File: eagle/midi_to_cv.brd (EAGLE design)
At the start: 100 x 80 mm, 73 parts, among them IC1 TL084P, IC2 4067N, IC3 4067N, IC4 TL072P, U1 ATMEGA328P_PDIP, U4 4584N

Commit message: parts basically on board and 072 powered
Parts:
- removed IC2, IC3: 4067N, 40xx:DIL24-6
- moved R27 249.5 mm to (91.4, 16.5)
- moved R29 249.5 mm to (72.4, 14.0)
- moved R28 242.3 mm to (72.4, 11.4)
- moved R18 238.0 mm to (91.4, 14.0)
- moved R10 233.4 mm to (91.4, 19.1), turned to 180 degrees
- moved R26 222.5 mm to (55.9, 6.35)
- moved R17 221.0 mm to (72.4, 8.89)
- moved R9 218.5 mm to (62.2, 20.3), turned to 180 degrees
- moved LED2 212.4 mm to (81.3, 20.3), turned to 180 degrees
- moved IC4 208.5 mm to (87.6, 7.62)
- moved R19 197.5 mm to (40.6, 38.1)
- moved LED1 189.2 mm to (72.4, 3.81), turned to 180 degrees
- moved MOUT_P5 188.9 mm to (43.2, 34.3)
- moved R23 174.7 mm to (3.81, 14.0), turned to 90 degrees
- moved MOUT_P4 170.2 mm to (3.81, 22.9)
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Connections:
- removed net V+: IC4.8
- removed net V-: IC4.4
- net +5V: now also IC4.8; no longer IC2.24, IC3.24
- net GND: now also IC4.4; no longer IC2.12, IC3.12

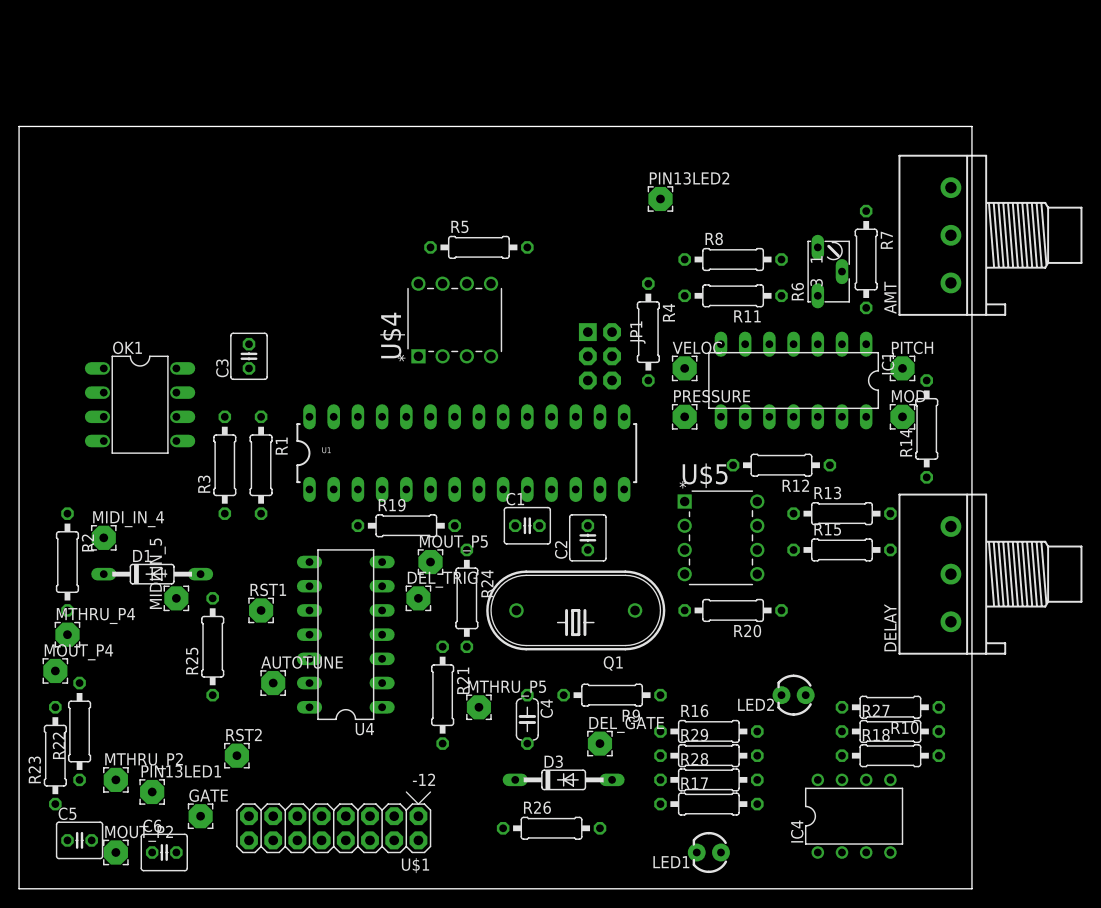
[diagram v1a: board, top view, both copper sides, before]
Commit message: swapped some gates and rearranged to layout
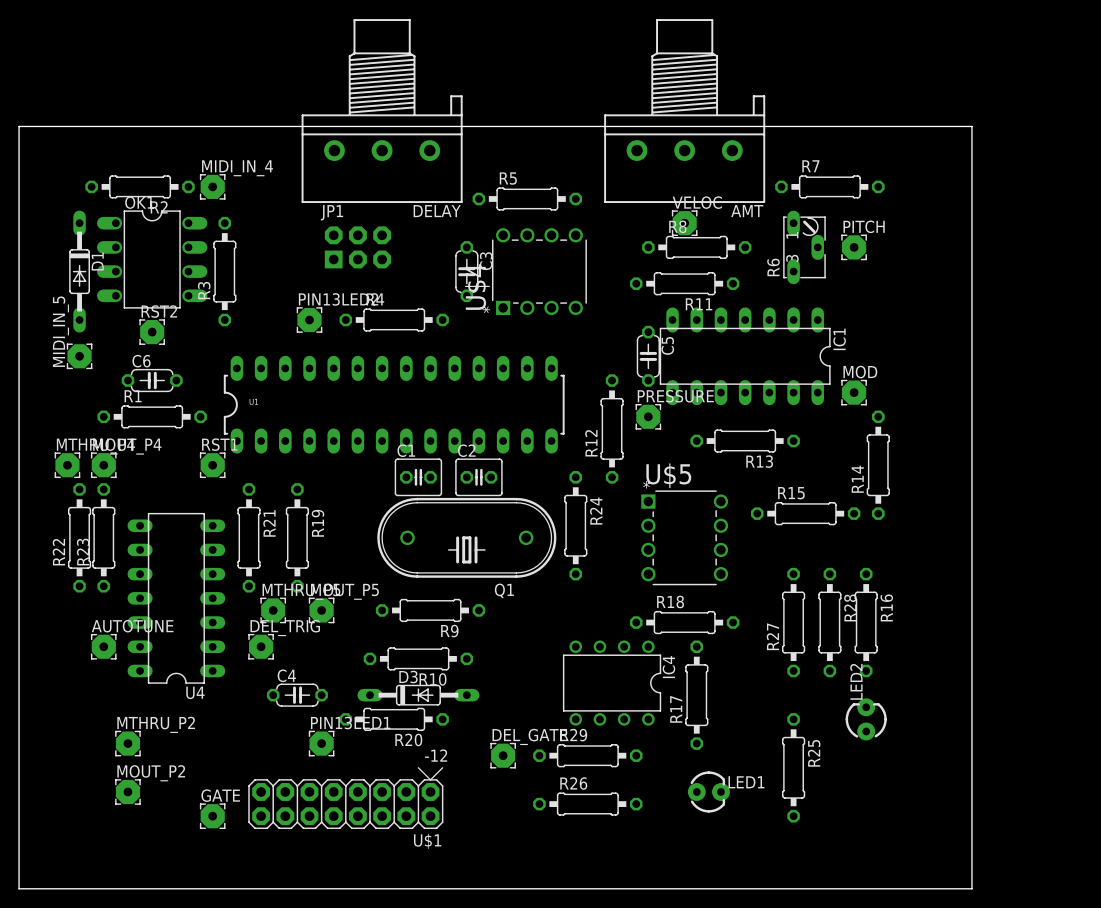
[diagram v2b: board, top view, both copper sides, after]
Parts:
- C3, C5, C6: device rcl:C025-040X050 -> rcl:C050-024X044
- moved C5 78.4 mm to (66.0, 55.9), turned to 270 degrees
- moved DELAY 74.4 mm to (38.1, 77.5), turned to 180 degrees
- moved R25 62.3 mm to (81.3, 12.7), turned to 270 degrees
- moved R10 49.8 mm to (41.9, 24.1)
- moved C6 49.5 mm to (14.0, 53.3)
- moved RST2 45.3 mm to (14.0, 58.4)
- moved R2 40.1 mm to (12.7, 73.7), turned to 180 degrees
- moved PIN13LED2 39.0 mm to (30.5, 59.7)
- moved MIDI_IN_4 38.6 mm to (20.3, 73.7)
- moved R20 37.4 mm to (39.4, 17.8)
- moved D1 32.7 mm to (6.35, 64.8), turned to 270 degrees
- moved AMT 29.3 mm to (69.8, 77.5), turned to 180 degrees
- moved IC4 29.0 mm to (62.2, 21.6), turned to 180 degrees
- moved JP1 27.9 mm to (35.6, 67.3), turned to 0 degrees
- moved MIDI_IN_5 27.4 mm to (6.35, 55.9)
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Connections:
- net N$39: now also U4.5; no longer U4.1
- net N$40: now also U4.2, U4.3; no longer U4.4, U4.5
- net N$41: now also U4.1; no longer U4.3
- net N$49: now also U4.4; no longer U4.6
- net N$50: now also U4.6; no longer U4.2

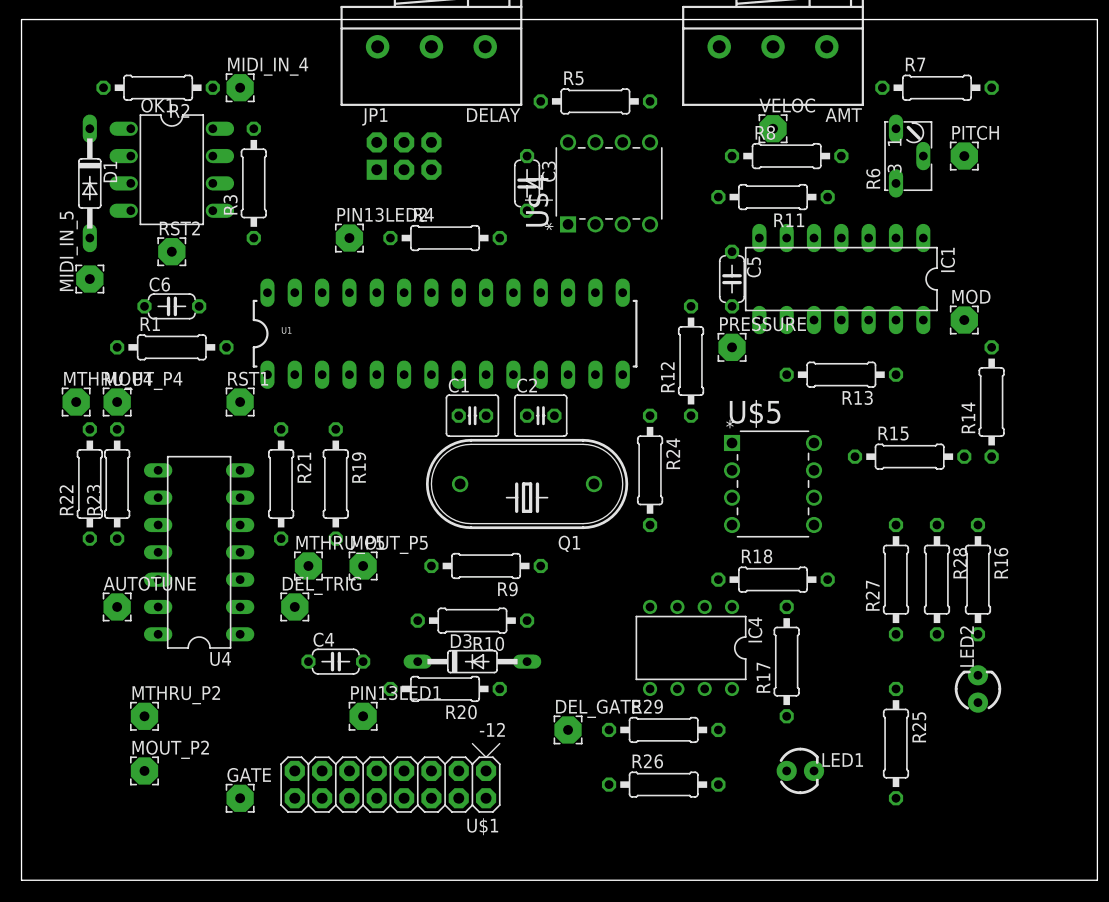
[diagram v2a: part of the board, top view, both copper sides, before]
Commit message: arranged power to the right and getting close to routed
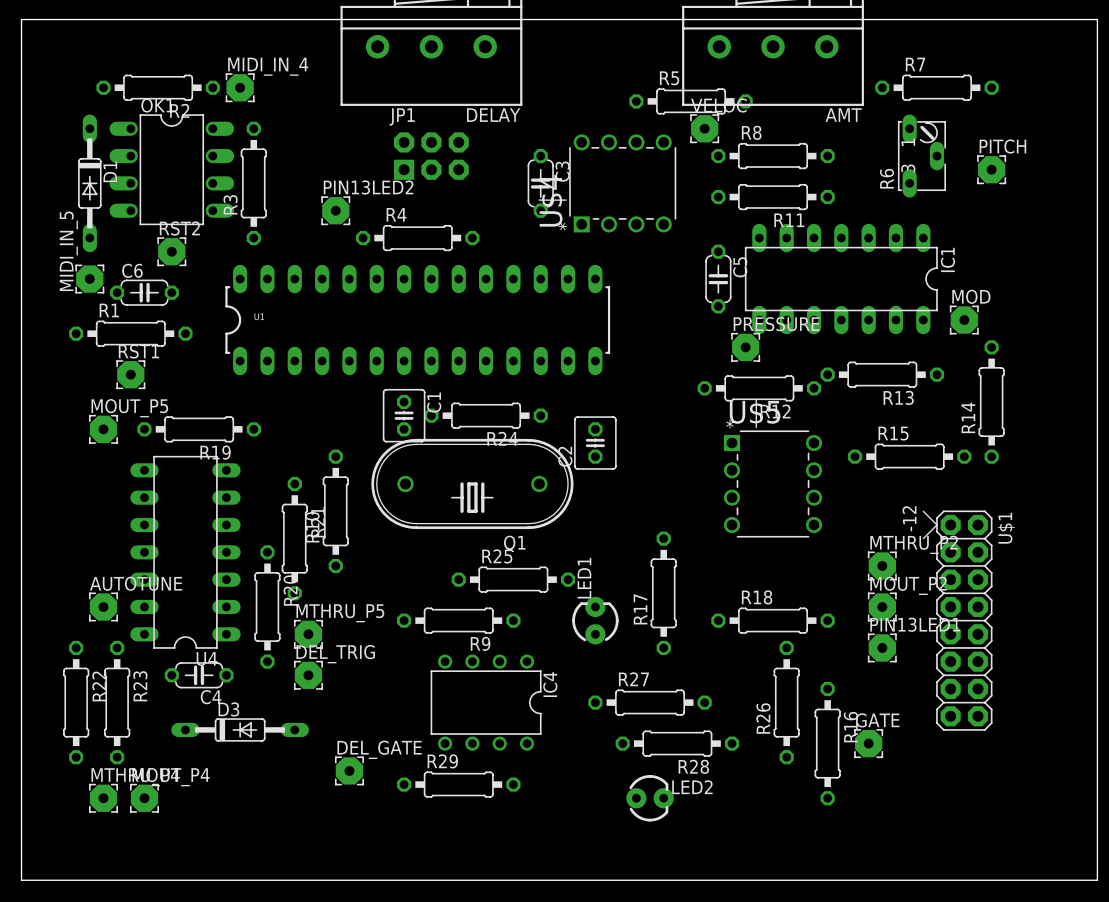
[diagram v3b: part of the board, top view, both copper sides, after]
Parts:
- moved MOUT_P2 70.3 mm to (80.0, 25.4)
- moved MTHRU_P2 70.0 mm to (80.0, 29.2)
- moved GATE 58.6 mm to (78.7, 12.7)
- moved U$1 53.8 mm to (87.6, 26.7), turned to 270 degrees
- moved PIN13LED1 48.7 mm to (80.0, 21.6)
- moved R25 38.7 mm to (45.7, 27.9), turned to 0 degrees
- moved MOUT_P4 36.9 mm to (11.4, 7.62)
- moved MTHRU_P4 36.9 mm to (7.62, 7.62)
- moved LED2 32.1 mm to (58.4, 7.62), turned to 0 degrees
- moved R28 28.5 mm to (61.0, 12.7), turned to 180 degrees
- moved MOUT_P5 27.3 mm to (7.62, 41.9)
- moved R27 25.6 mm to (58.4, 16.5), turned to 0 degrees
- moved LED1 23.6 mm to (53.3, 24.1), turned to 90 degrees
- moved D3 22.5 mm to (20.3, 14.0)
- moved R16 20.7 mm to (74.9, 12.7)
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
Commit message: ready to cut layout
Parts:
- R18, R27: value 20k -> 47k
- moved VELOC 23.2 mm to (85.3, 77.7)
- moved R10 15.4 mm to (32.8, 19.3)
- moved R27 6.48 mm to (52.1, 15.2), turned to 90 degrees
- moved R17 6.36 mm to (59.4, 20.3)
- moved R5 3.07 mm to (65.0, 73.7)
- moved R12 2.54 mm to (71.1, 45.7)
- moved LED1 2.54 mm to (54.9, 26.2)
- moved R18 2.41 mm to (70.6, 26.4)
- moved DEL_GATE 2.05 mm to (28.4, 9.91)
- moved MOUT_P5 1.93 mm to (8.38, 43.7)
- moved R13 1.83 mm to (78.5, 48.0)
- moved U$5 1.80 mm to (72.4, 31.8)
- moved R1 1.70 mm to (8.64, 50.0)
- moved C2 1.55 mm to (53.6, 39.1)
- moved RST1 1.55 mm to (11.7, 46.7)
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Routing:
- net GND: track 0.00 -> 489.9 mm
- net +5V: track 0.00 -> 300.3 mm, vias 0 -> 2
- net +12V: track 0.00 -> 96.5 mm
- net N$9: track 0.00 -> 71.3 mm
- net N$43: track 0.00 -> 60.9 mm, vias 0 -> 2
- net N$10: track 0.00 -> 57.3 mm
- net N$38: track 0.00 -> 55.0 mm, vias 0 -> 2
- net N$30: track 0.00 -> 50.3 mm, vias 0 -> 2
- net N$14: track 0.00 -> 47.5 mm
- net N$53: track 0.00 -> 44.4 mm
- net N$26: track 0.00 -> 43.4 mm, vias 0 -> 4
- net N$45: track 0.00 -> 38.4 mm
- net N$24: track 0.00 -> 38.3 mm
- net N$16: track 0.00 -> 36.4 mm
- net N$15: track 0.00 -> 32.6 mm
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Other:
- board size 100 x 80 mm -> 100 x 80.8 mm
